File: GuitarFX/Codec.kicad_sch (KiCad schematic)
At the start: 35 parts, among them IC401 PCM3060PWR, U1 CS4272

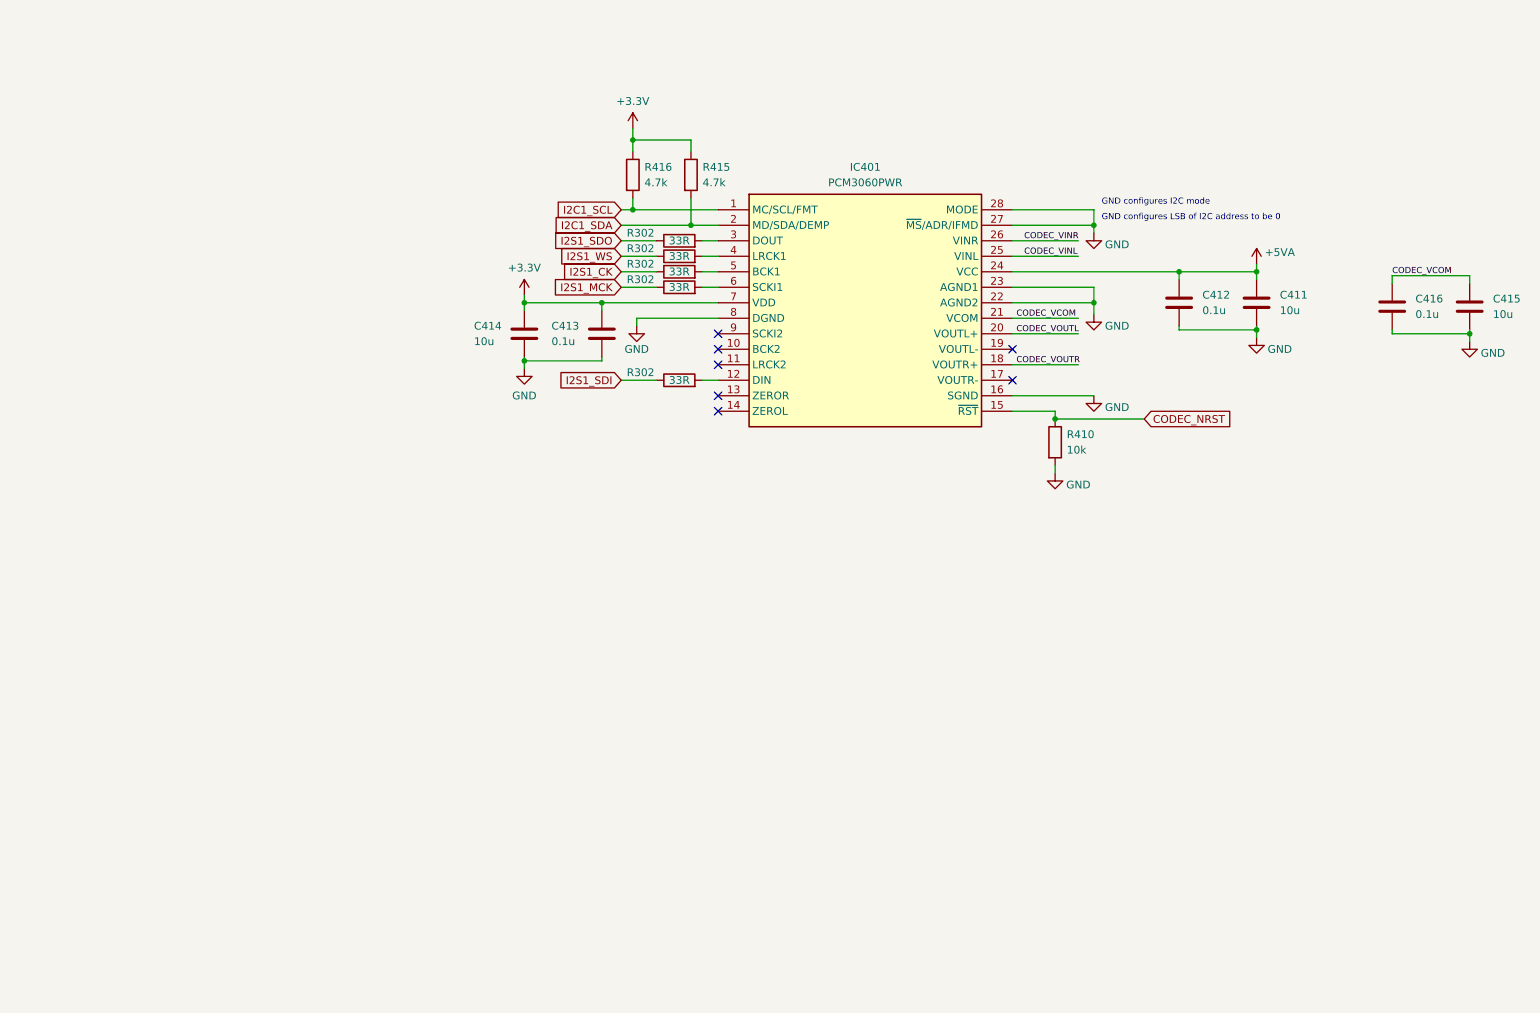
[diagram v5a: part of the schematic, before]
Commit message: Refactored CODEC and added opamp for analog front end
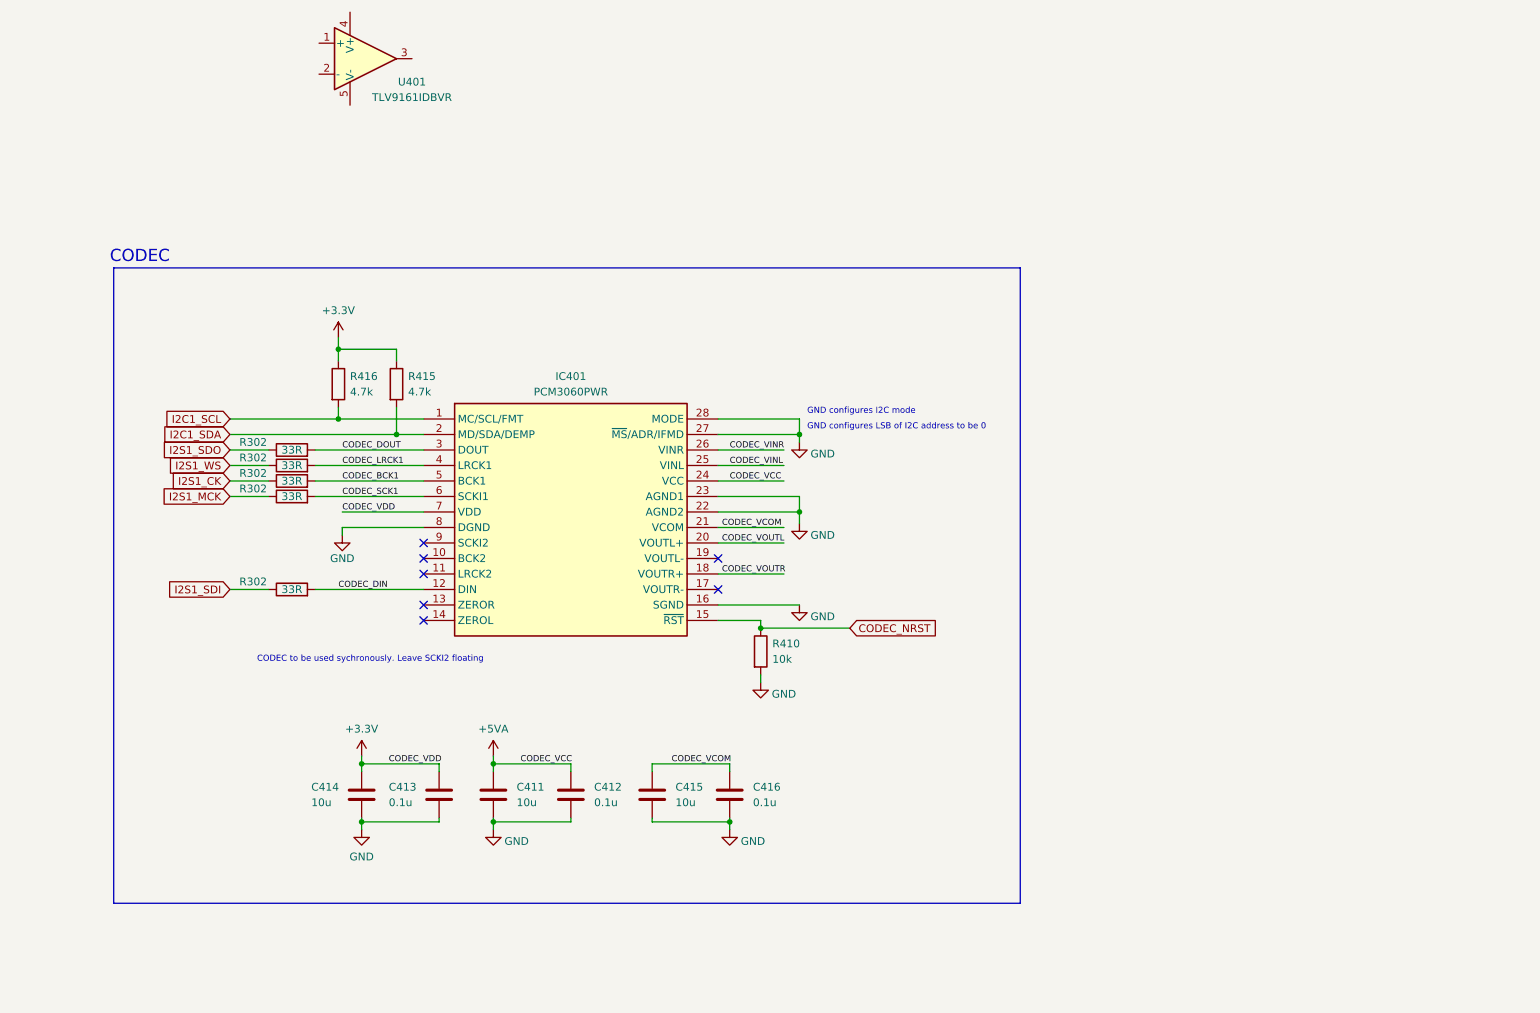
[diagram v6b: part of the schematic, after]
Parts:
- added U401: TLV9161IDBVR, TLV9161IDBVR:SOT95P280X145-5N, symbol Simulation_SPICE:OPAMP
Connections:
- net CODEC_DOUT: now reaches IC401.3 (DOUT), R302.2
- net CODEC_BCK1: now reaches IC401.5 (BCK1), R302.2
- net CODEC_DIN: now reaches IC401.12 (DIN), R302.2
- net CODEC_LRCK1: now reaches IC401.4 (LRCK1), R302.2
- net CODEC_SCK1: now reaches IC401.6 (SCKI1), R302.2
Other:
- note added: "CODEC"
- note added: "CODEC to be used sychronously. Leave SCKI2 floating"
- moved on the sheet: C413, C414, IC401, R302, R410, R415, R416

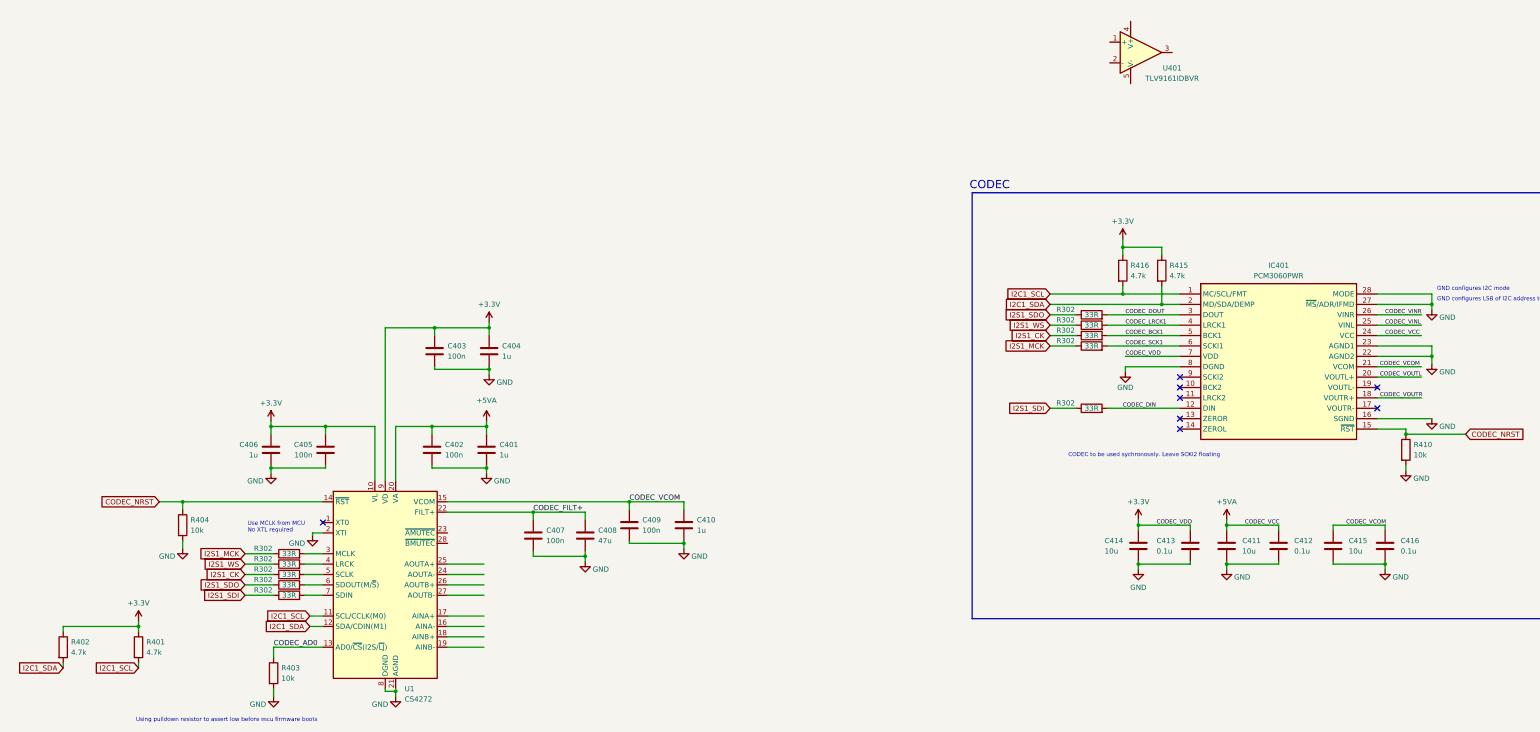
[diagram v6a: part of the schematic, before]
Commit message: Added RGB LEDs and ADC connections for potentiometer readings along with connector
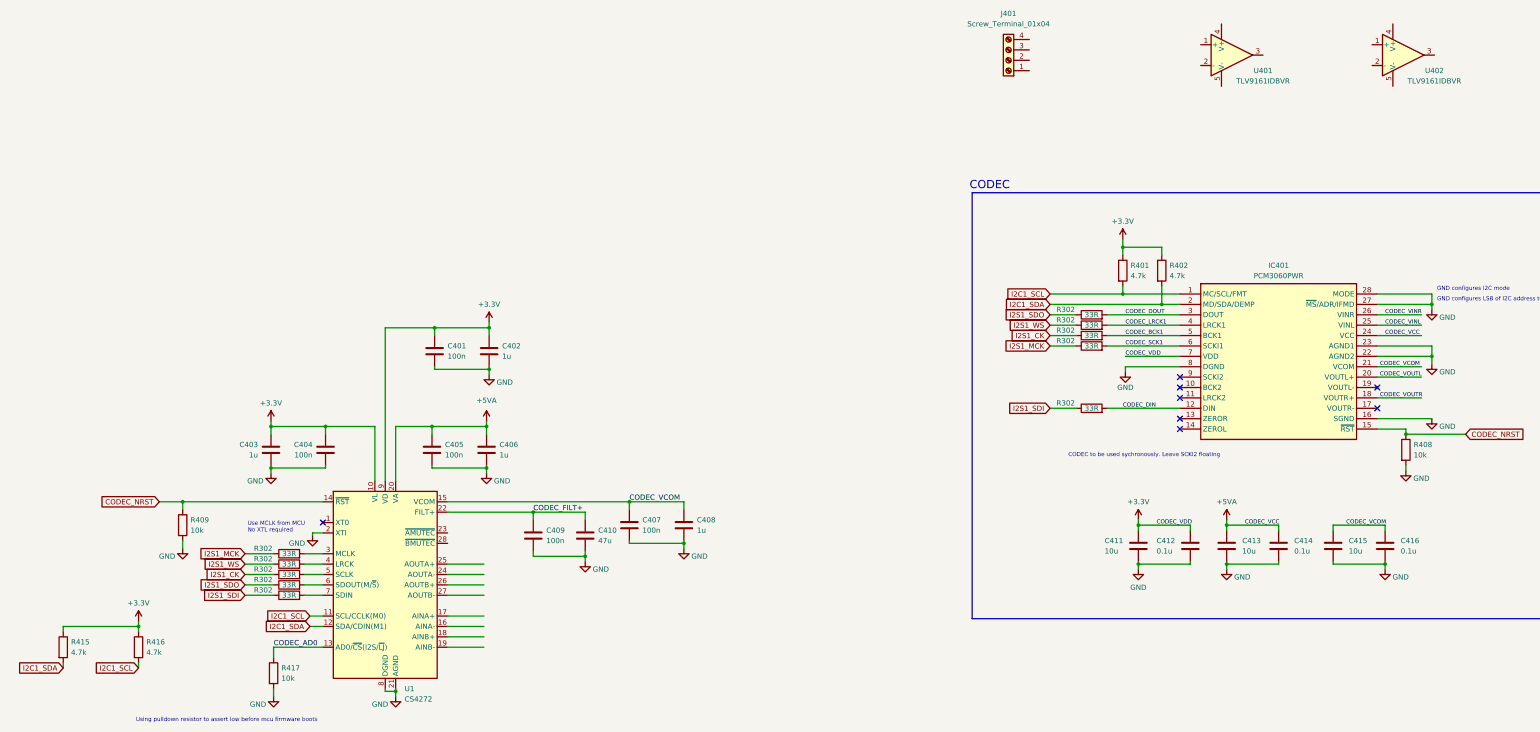
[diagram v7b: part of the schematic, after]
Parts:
- added J401: Screw_Terminal_01x04, symbol Connector:Screw_Terminal_01x04
- added U402: TLV9161IDBVR, TLV9161IDBVR:SOT95P280X145-5N, symbol Simulation_SPICE:OPAMP
- renumbered C403 to C401, C404 to C402, C406 to C403, C405 to C404, C402 to C405, C401 to C406, C409 to C407, C410 to C408, C407 to C409, C408 to C410, C414 to C411, C413 to C412, C411 to C413, C412 to C414, R416 to R401, R415 to R402, R410 to R408, R404 to R409, R402 to R415, R401 to R416, R403 to R417
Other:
- moved on the sheet: U401

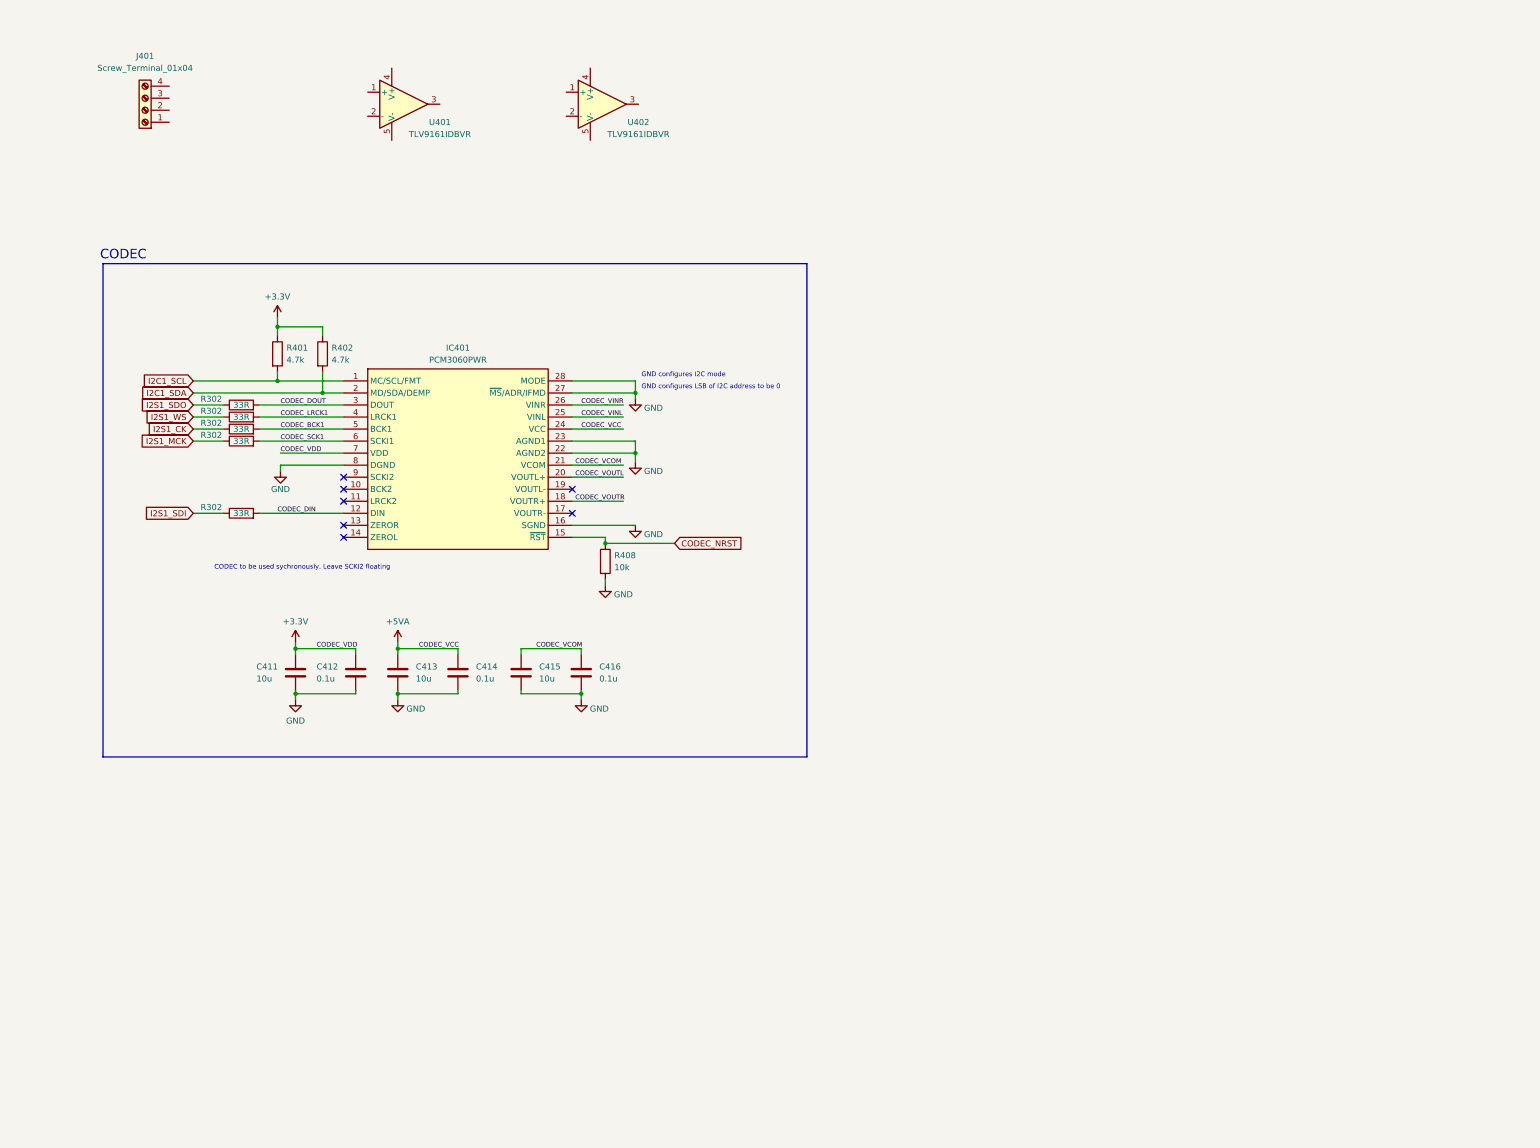
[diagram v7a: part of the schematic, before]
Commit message: Completed Analog Frontend schematic
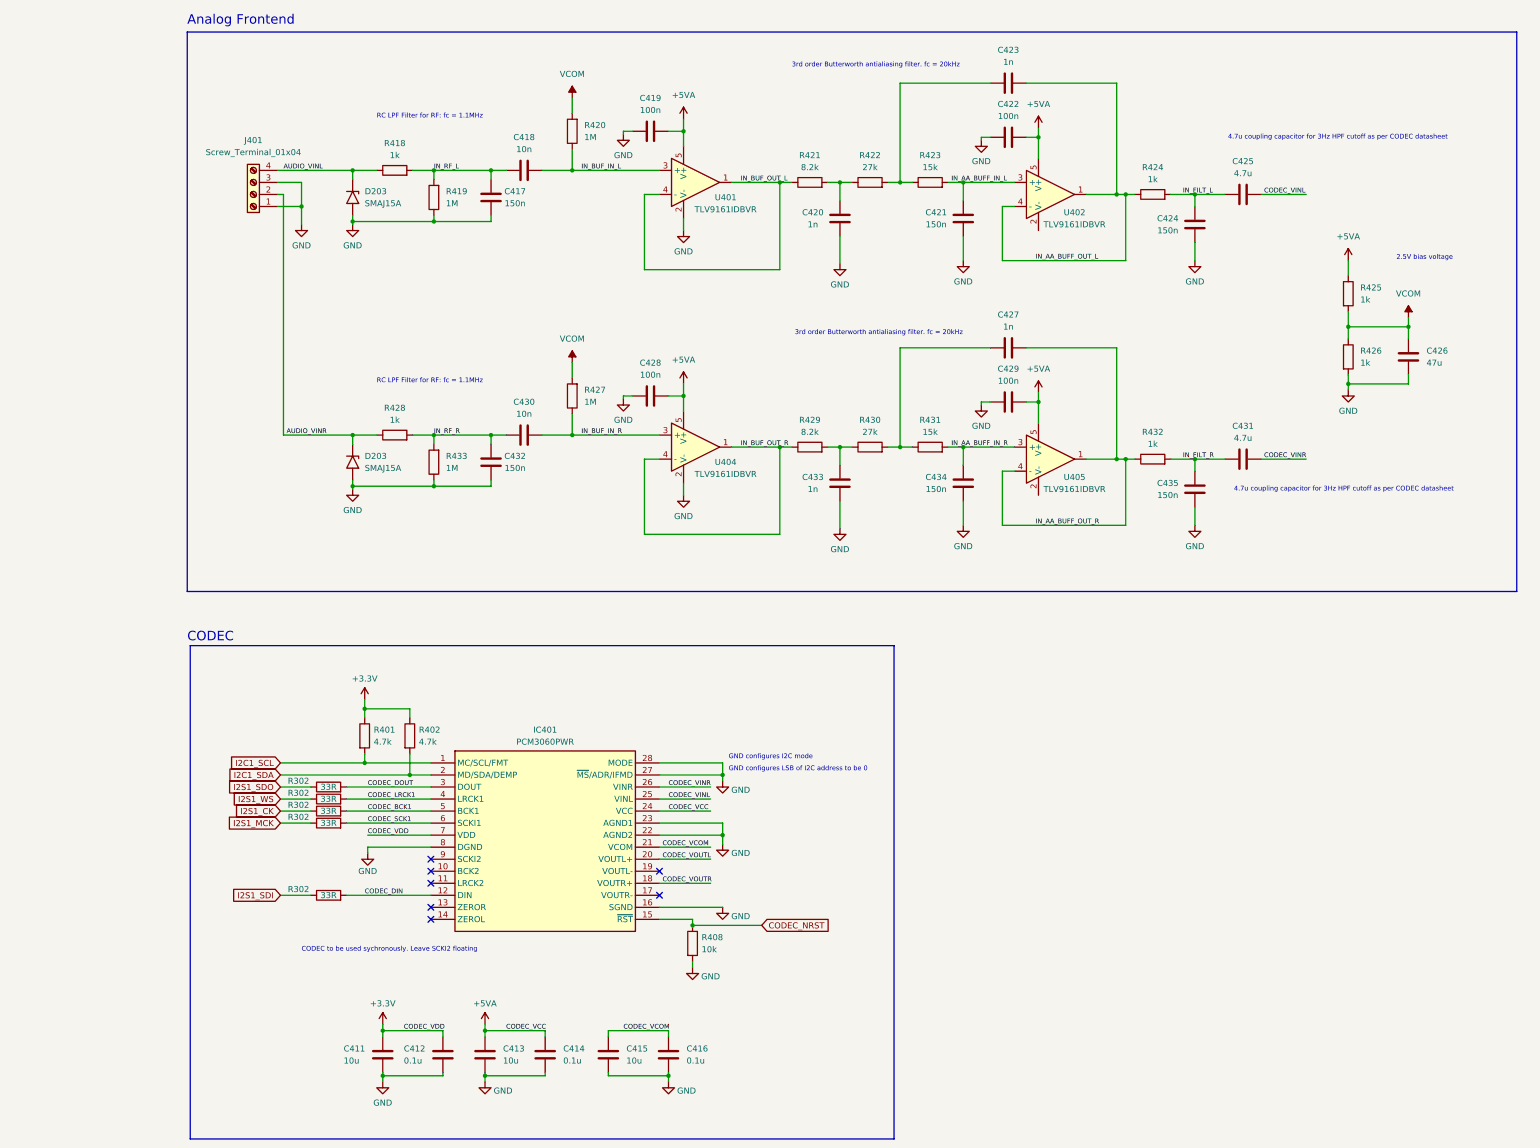
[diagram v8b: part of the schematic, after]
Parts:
- added C417, C421, C424, C432, C434, C435: 150n, symbol Device:C
- added C418, C430: 10n, symbol Device:C
- added C419, C422, C428, C429: 100n, symbol Device:C
- added C420, C423, C427, C433: 1n, symbol Device:C
- added C425, C431: 4.7u, symbol Device:C
- added C426: 47u, symbol Device:C
- added D203 (x2): SMAJ15A, Diode_SMD:D_SMA, symbol Diode:SMAJ15A
- added R418, R424, R425, R426, R428, R432: 1k, symbol Device:R
- added R419, R420, R427, R433: 1M, symbol Device:R
- added R421, R429: 8.2k, symbol Device:R
- added R422, R430: 27k, symbol Device:R
- added R423, R431: 15k, symbol Device:R
- added U404, U405: TLV9161IDBVR, SOT95P280X145-5N, symbol TLV9161IDBVR:TLV9161IDBVR
- U401, U402: footprint TLV9161IDBVR:SOT95P280X145-5N -> SOT95P280X145-5N; symbol Simulation_SPICE:OPAMP -> TLV9161IDBVR:TLV9161IDBVR; Arrow Part Number (none) -> TLV9161IDBVR; Arrow Price/Stock (none) -> https://www.arrow.com/en/products/tlv9161idbvr/texas-instru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; Height (none) -> 1.45; Manufacturer_Name (none) -> Texas Instruments; Manufacturer_Part_Number (none) -> TLV9161IDBVR; Mouser Part Number (none) -> 595-TLV9161IDBVR; Mouser Price/Stock (none) -> https://www.mouser.co.uk/ProductDetail/Texas-Instruments/TL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
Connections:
- net +5VA: now also U401.5 (V+), U402.5 (V+), C419.1, C422.1, C428.1, C429.1, R425.1, U404.5 (V+), U405.5 (V+)
- net CODEC_VINL: now also C425.1
- net CODEC_VINR: now also C431.1
- net GND: now also J401.1 (Pin_1), J401.3 (Pin_3), U401.2 (V-), C417.2, C419.2, C420.2, C421.2, C422.2, C424.2, C426.2, C428.2, C429.2, C432.2, C433.2, C434.2, C435.2, D203.2 (A2), D203.2 (A2), R419.1, R426.2, R433.1, U404.2 (V-)
- net IN_BUF_OUT_L: now reaches U401.1
- net IN_BUF_OUT_L: now also U401.4 (-), R421.1
- net IN_BUF_IN_L: now reaches U401.3 (+)
- net IN_BUF_IN_L: now also C418.2, R420.1
- net IN_AA_BUFF_OUT_L: now reaches U402.1
- net IN_AA_BUFF_OUT_L: now also U402.4 (-), C423.1, R424.1
- net IN_AA_BUFF_IN_L: now reaches U402.3 (+)
- net IN_AA_BUFF_IN_L: now also C421.1, R423.2
- net AUDIO_VINR: now reaches J401.2 (Pin_2)
- net AUDIO_VINR: now also D203.1 (A1), R428.1
- net AUDIO_VINL: now reaches J401.4 (Pin_4)
- net AUDIO_VINL: now also D203.1 (A1), R418.1
- new net: C423.2, R422.2, R423.1
- new net: C433.1, R429.2, R430.1
- new net: C427.2, R430.2, R431.1
- new net: C420.1, R421.2, R422.1
- new net IN_AA_BUFF_IN_R: C434.1, R431.2, U405.3 (+)
- new net IN_AA_BUFF_OUT_R: C427.1, R432.1, U405.1, U405.4 (-)
- new net IN_BUF_IN_R: C430.2, R427.1, U404.3 (+)
- new net IN_BUF_OUT_R: R429.1, U404.1, U404.4 (-)
- new net IN_FILT_L: C424.1, C425.2, R424.2
- new net IN_FILT_R: C431.2, C435.1, R432.2
- new net IN_RF_L: C417.1, C418.1, R418.2, R419.2
- new net IN_RF_R: C430.1, C432.1, R428.2, R433.2
- new net VCOM: C426.1, R420.2, R425.2, R426.1, R427.2
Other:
- note added: "2.5V bias voltage"
- note added: "3rd order Butterworth antialiasing filter. fc = 20kHz"
- note added: "4.7u coupling capacitor for 3Hz HPF cutoff as per CODEC datasheet"
- note added: "Analog Frontend"
- note added: "RC LPF Filter for RF: fc = 1.1MHz"
- moved on the sheet: C411, C412, C413, C414, C415, C416, IC401, J401, R302, R401, R402, R408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
